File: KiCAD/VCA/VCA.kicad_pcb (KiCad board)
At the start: 2 copper layers, 30 x 100 mm, 18 parts, among them J1 VIN, J2 VC, J3 VOUT, J4 Conn_01x03_Pin, Q1 J172, Q2 J172, U1 LT1006

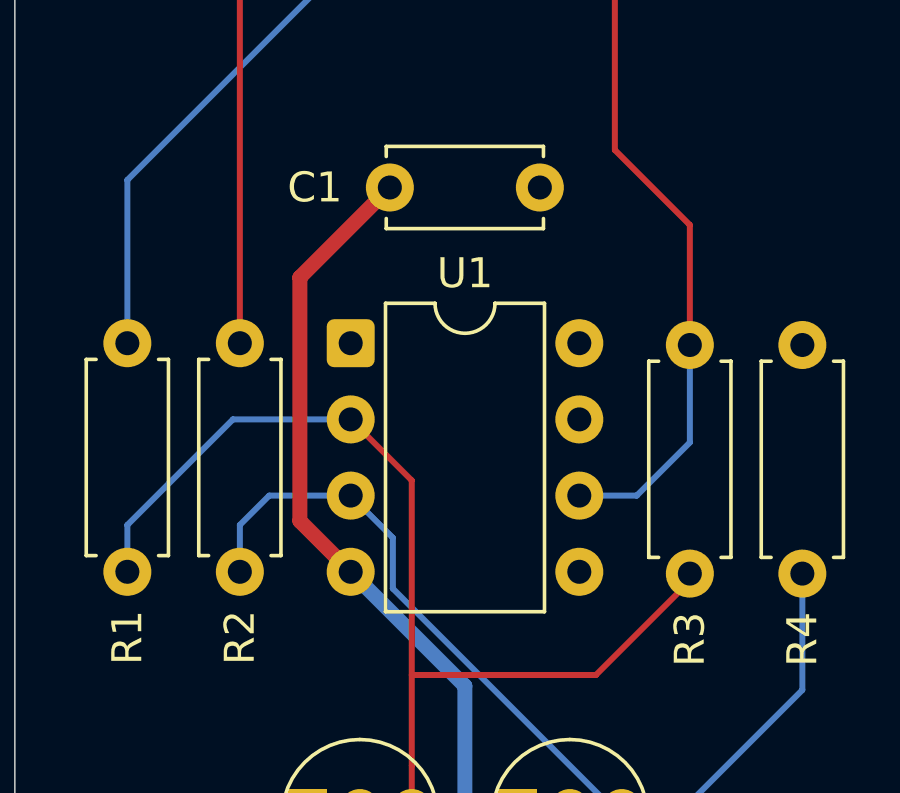
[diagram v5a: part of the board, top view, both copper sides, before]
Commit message: VCA Footprint update
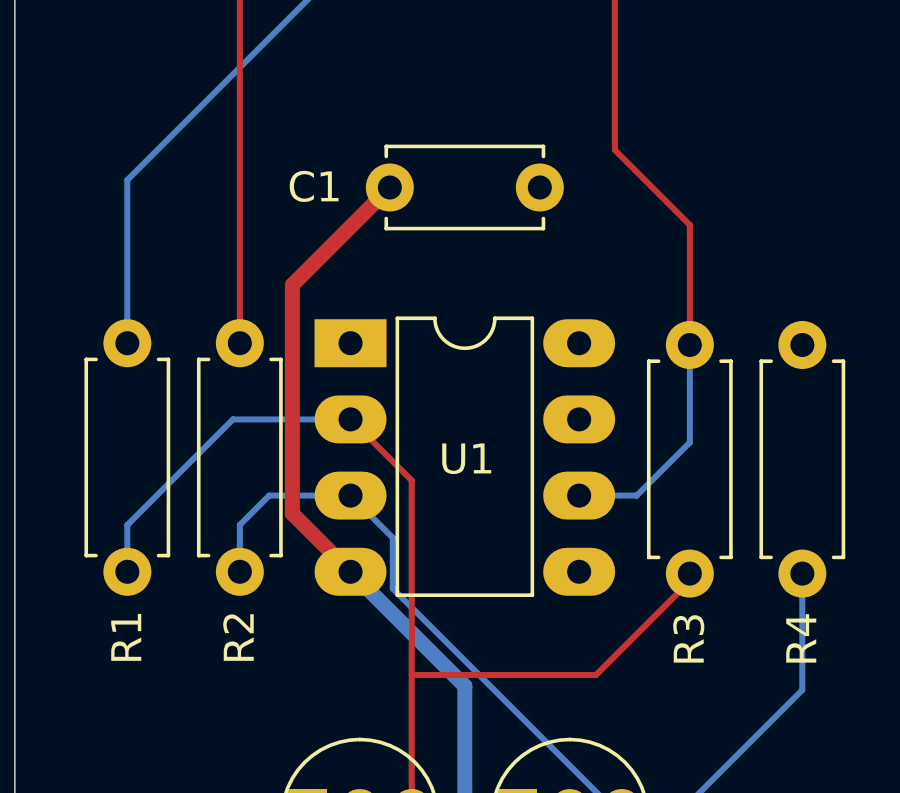
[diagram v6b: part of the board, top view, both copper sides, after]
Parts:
- U1: footprint Package_DIP:DIP-8_W7.62mm -> HackSynth:DIP-8_W7.62mm_LongPads
- moved U1 5.38 mm to (130.0, 98.0)
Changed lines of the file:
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@@
 		)
 	)
-	(footprint "Package_DIP:DIP-8_W7.62mm"
+	(footprint "HackSynth:DIP-8_W7.62mm_LongPads"
 		(layer "F.Cu")
-		(at 126.195 94.190001)
-		(descr "8-lead though-hole mounted DIP package, row spacing 7.62mm (300 mils)")
-		(tags "THT DIP DIL PDIP 2.54mm 7.62mm 300mil")
+		(at 130 98)
+		(descr "8-lead though-hole mounted DIP package, row spacing 7.62 mm (300 mils), LongPads")
+		(tags "THT DIP DIL PDIP 2.54mm 7.62mm 300mil LongPads")
 		(property "Reference" "U1"
-			(at 3.81 -2.33 0)
+			(at 0.065 0.07 0)
 			(layer "F.SilkS")
 			(effects
@@
 		)
 		(property "Value" "LT1006"
-			(at 3.81 9.95 0)
+			(at 0 6.14 0)
 			(layer "F.Fab")
 			(effects
@@
 		(attr through_hole)
 		(fp_line
-			(start 1.16 -1.33)
-			(end 1.16 8.95)
+			(start -2.25 -4.64)
+			(end -2.25 4.59)
 			(stroke
 				(width 0.12)
@@
 		)
 		(fp_line
-			(start 1.16 8.95)
-			(end 6.46 8.95)
+			(start -2.25 4.59)
+			(end 2.25 4.59)
 			(stroke
 				(width 0.12)
@@
 		)
 		(fp_line
-			(start 2.81 -1.33)
-			(end 1.16 -1.33)
+			(start -1 -4.64)
+			(end -2.25 -4.64)
 			(stroke
 				(width 0.12)
@@
 		)
 		(fp_line
-			(start 6.46 -1.33)
-			(end 4.81 -1.33)
+			(start 2.25 -4.64)
+			(end 1 -4.64)
 			(stroke
 				(width 0.12)
@@
 		)
 		(fp_line
-			(start 6.46 8.95)
-			(end 6.46 -1.33)
+			(start 2.25 4.59)
+			(end 2.25 -4.64)
 			(stroke
 				(width 0.12)
@@
 		)
 		(fp_arc
-			(start 4.81 -1.33)
-			(mid 3.81 -0.33)
-			(end 2.81 -1.33)
+			(start 1 -4.64)
+			(mid 0 -3.64)
+			(end -1 -4.64)
 			(stroke
 				(width 0.12)
@@
 			(layer "F.SilkS")
 		)
-		(fp_rect
-			(start -1.06 -1.52)
-			(end 8.67 9.14)
+		(fp_line
+			(start 0 -0.75)
+			(end 0 0.75)
+			(stroke
+				(width 0.05)
+				(type solid)
+			)
+			(layer "Dwgs.User")
+		)
+		(fp_line
+			(start 0.75 0)
+			(end -0.75 0)
+			(stroke
+				(width 0.05)
+				(type solid)
+			)
+			(layer "Dwgs.User")
+		)
+		(fp_line
+			(start -5.26 -5.36)
+			(end -5.26 5.34)
 			(stroke
 				(width 0.05)
 				(type solid)
 			)
-			(fill no)
 			(layer "F.CrtYd")
 		)
 		(fp_line
-			(start 0.635 -0.27)
-			(end 1.635 -1.27)
+			(start -5.26 5.34)
+			(end 5.29 5.34)
 			(stroke
-				(width 0.1)
+				(width 0.05)
 				(type solid)
 			)
-			(layer "F.Fab")
+			(layer "F.CrtYd")
+		)
+		(fp_line
+			(start 5.29 -5.36)
+			(end -5.26 -5.36)
+			(stroke
+				(width 0.05)
+				(type solid)
+			)
+			(layer "F.CrtYd")
+		)
+		(fp_line
+			(start 5.29 5.34)
+			(end 5.29 -5.36)
+			(stroke
+				(width 0.05)
+				(type solid)
+			)
+			(layer "F.CrtYd")
 		)
 		(fp_line
-			(start 0.635 8.89)
-			(end 0.635 -0.27)
+			(start -3.175 -4.08)
+			(end -2.175 -5.08)
 			(stroke
 				(width 0.1)
@@
 		)
 		(fp_line
-			(start 1.635 -1.27)
-			(end 6.985 -1.27)
+			(start -3.175 5.08)
+			(end -3.175 -4.08)
 			(stroke
 				(width 0.1)
@@
 		)
 		(fp_line
-			(start 6.985 -1.27)
-			(end 6.985 8.89)
+			(start -2.175 -5.08)
+			(end 3.175 -5.08)
 			(stroke
 				(width 0.1)
@@
 		)
 		(fp_line
-			(start 6.985 8.89)
-			(end 0.635 8.89)
+			(start 3.175 -5.08)
+			(end 3.175 5.08)
 			(stroke
 				(width 0.1)
@@
 			(layer "F.Fab")
 		)
-		(fp_text user "${REFERENCE}"
-			(at 3.81 3.81 90)
-			(layer "F.Fab")
-			(effects
-				(font
-					(size 1 1)
-					(thickness 0.15)
-				)
+		(fp_line
+			(start 3.175 5.08)
+			(end -3.175 5.08)
+			(stroke
+				(width 0.1)
+				(type solid)
 			)
+			(layer "F.Fab")
 		)
-		(pad "1" thru_hole roundrect
-			(at 0 0)
-			(size 1.6 1.6)
+		(pad "1" thru_hole rect
+			(at -3.81 -3.81)
+			(size 2.4 1.6)
 			(drill 0.8)
 			(layers "*.Cu" "*.Mask")
 			(remove_unused_layers no)
-			(roundrect_rratio 0.15625)
 			(net 14 "unconnected-(U1-NC-Pad1)")
 			(pinfunction "NC")
 			(pintype "no_connect")
 		)
-		(pad "2" thru_hole circle
-			(at 0 2.54)
-			(size 1.6 1.6)
+		(pad "2" thru_hole oval
+			(at -3.81 -1.27)
+			(size 2.4 1.6)
 			(drill 0.8)
 			(layers "*.Cu" "*.Mask")
@@
 			(pintype "input")
 		)
-		(pad "3" thru_hole circle
-			(at 0 5.08)
-			(size 1.6 1.6)
+		(pad "3" thru_hole oval
+			(at -3.81 1.27)
+			(size 2.4 1.6)
 			(drill 0.8)
 			(layers "*.Cu" "*.Mask")
@@
 			(pintype "input")
 		)
-		(pad "4" thru_hole circle
-			(at 0 7.62)
-			(size 1.6 1.6)
+		(pad "4" thru_hole oval
+			(at -3.81 3.81)
+			(size 2.4 1.6)
 			(drill 0.8)
 			(layers "*.Cu" "*.Mask")
@@
 			(pintype "power_in")
 		)
-		(pad "5" thru_hole circle
-			(at 7.62 7.62)
-			(size 1.6 1.6)
+		(pad "5" thru_hole oval
+			(at 3.81 3.81)
+			(size 2.4 1.6)
 			(drill 0.8)
 			(layers "*.Cu" "*.Mask")
@@
 			(pintype "no_connect")
 		)
-		(pad "6" thru_hole circle
-			(at 7.62 5.08)
-			(size 1.6 1.6)
+		(pad "6" thru_hole oval
+			(at 3.81 1.27)
+			(size 2.4 1.6)
 			(drill 0.8)
 			(layers "*.Cu" "*.Mask")
@@
 			(pintype "output")
 		)
-		(pad "7" thru_hole circle
-			(at 7.62 2.54)
-			(size 1.6 1.6)
+		(pad "7" thru_hole oval
+			(at 3.81 -1.27)
+			(size 2.4 1.6)
 			(drill 0.8)
 			(layers "*.Cu" "*.Mask")
@@
 			(pintype "power_in")
 		)
-		(pad "8" thru_hole circle
-			(at 7.62 0)
-			(size 1.6 1.6)
+		(pad "8" thru_hole oval
+			(at 3.81 -3.81)
+			(size 2.4 1.6)
 			(drill 0.8)
 			(layers "*.Cu" "*.Mask")
@@
 		)
 		(embedded_fonts no)
-		(model "${KICAD9_3DMODEL_DIR}/Package_DIP.3dshapes/DIP-8_W7.62mm.step"
+		(model "C:/Users/ocd/OneDrive/Drafting/CCHS/HackSynth/KiCAD/HackSynth.pretty/DIP-8_W7.62mm.step"
 			(offset
-				(xyz 0 0 0)
+				(xyz -3.81 3.81 0)
 			)
 			(scale
@@
 	)
 	(segment
-		(start 124.5 100.115001)
-		(end 124.5 92.000001)
+		(start 124.25 92.250001)
+		(end 127.5 89.000001)
 		(width 0.5)
 		(layer "F.Cu")
@@
 	)
 	(segment
-		(start 124.5 92.000001)
-		(end 127.5 89.000001)
+		(start 124.25 99.87)
+		(end 124.25 92.250001)
 		(width 0.5)
 		(layer "F.Cu")
@@
 	)
 	(segment
-		(start 126.195 101.810001)
-		(end 124.5 100.115001)
+		(start 126.19 101.81)
+		(end 124.25 99.87)
 		(width 0.5)
 		(layer "F.Cu")

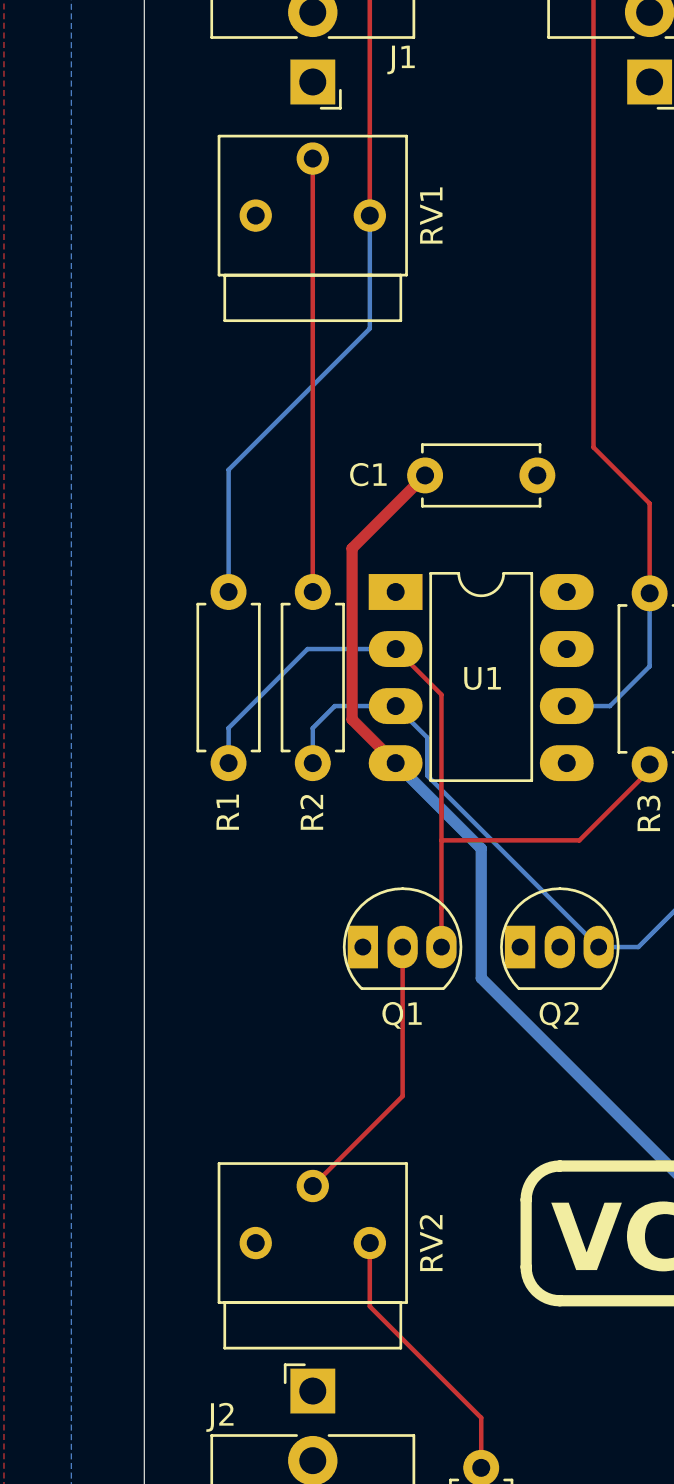
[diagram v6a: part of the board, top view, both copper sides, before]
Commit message: Footprint Edits
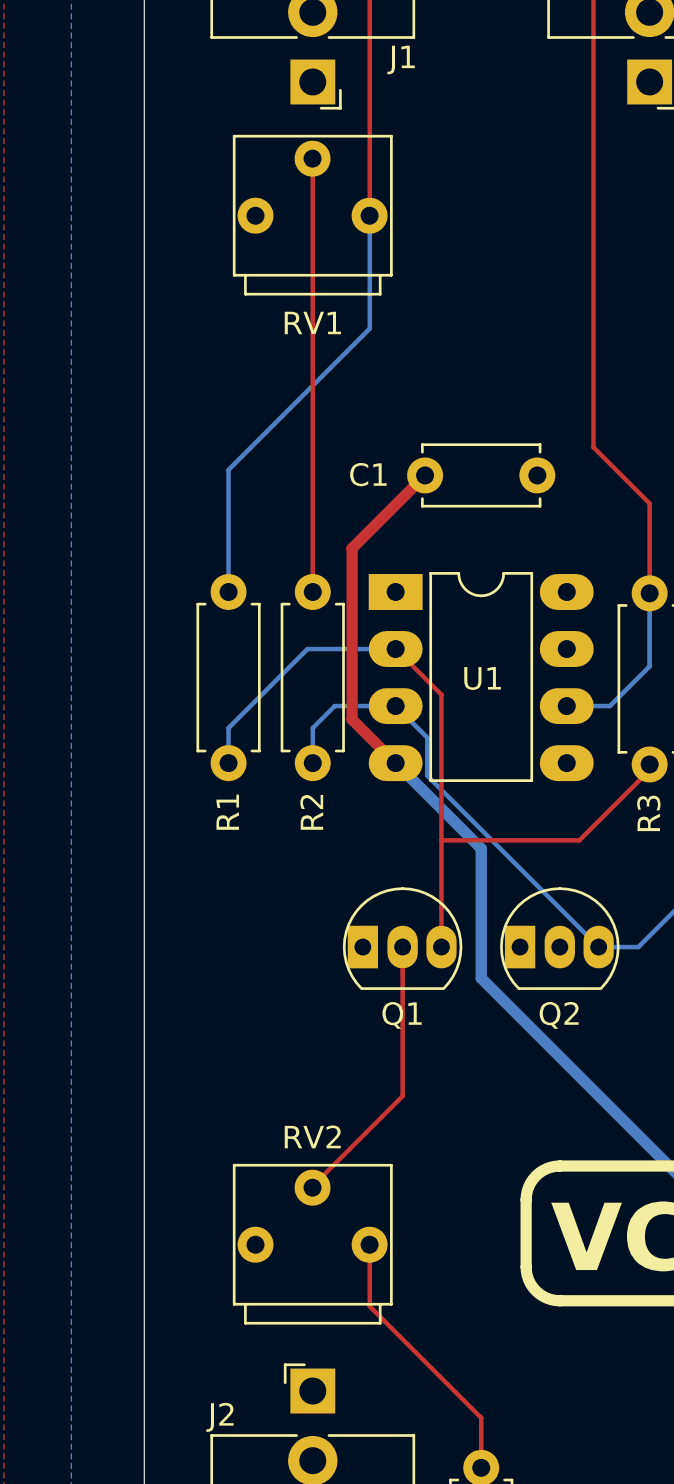
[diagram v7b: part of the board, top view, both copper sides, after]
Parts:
- moved RV2 2.54 mm to (122.5, 123.2), turned to 0 degrees
- moved RV1 2.54 mm to (122.5, 77.4), turned to 0 degrees
